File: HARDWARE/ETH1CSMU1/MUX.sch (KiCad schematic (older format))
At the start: 42 parts, among them J1401 Conn_01x03, K1401 MS05-1A87-75D, K1402 MS05-1A87-75D, K1403 MS05-1A87-75D, K1404 MS05-1A87-75D, K1405 MS05-1A87-75D, K1406 MS05-1A87-75D, K1407 MS05-1A87-75D, K1408 MS05-1A87-75D, K1409 MS05-1A87-75D, K1410 MS05-1A87-75D, K1411 MS05-1A87-75D, K1412 MS05-1A87-75D, K1413 MS05-1A87-75D, K1414 MS05-1A87-75D, K1415 MS05-1A87-75D, K1416 MS05-1A87-75D, K1417 MS05-1A87-75D, K1418 MS05-1A87-75D, K1419 G6KU-2F-Y, Q1401 BC847

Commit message: Schematic development
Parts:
- added C1301, C1302, C1303, C1304, C1305, C1306, C1307, C1308, C1309: 100n, symbol Device:C
- added R1301: R, symbol Device:R
- added U1301, U1302, U1303: TCA9534, symbol Interface_Expansion:TCA9534
- added U1304, U1305, U1306: ADG3308, symbol VoltageLevel_local:ADG3308
- added U1307: ULN2002, symbol Transistor_Array:ULN2002
- gave numbers to parts that had none: 2
- renumbered D1419 to D1301, D1401 to D1302, D1402 to D1303, D1403 to D1304, D1404 to D1305, D1405 to D1306, D1406 to D1307, D1407 to D1308, D1408 to D1309, D1409 to D1310, D1410 to D1311, D1411 to D1312, D1412 to D1313, D1413 to D1314, D1414 to D1315, D1415 to D1316, D1416 to D1317, D1417 to D1318, D1418 to D1319, J1401 to J1301, K1419 to K1301, K1401 to K1302, K1402 to K1303, K1403 to K1304, K1404 to K1305, K1405 to K1306, K1406 to K1307, K1407 to K1308, K1408 to K1309, K1409 to K1310, K1410 to K1311, K1411 to K1312, K1412 to K1313, K1413 to K1314, K1414 to K1315, K1415 to K1316, K1416 to K1317, K1417 to K1318, K1418 to K1319, Q1401 to Q1301
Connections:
- net +5V: now also C1301.1, C1302.1, C1303.1, U1304.20 (VCCY), U1305.20 (VCCY), U1306.20 (VCCY), U1307.9 (COM)
- net GND: now also C1301.2, C1302.2, C1303.2, C1304.2, C1305.2, C1306.2, C1307.2, C1308.2, C1309.2, U1301.2 (A1), U1301.3 (A2), U1301.8 (GND), U1302.1 (A0), U1302.3 (A2), U1302.8 (GND), U1303.3 (A2), U1303.8 (GND), U1304.11 (GND), U1305.11 (GND), U1306.11 (GND), U1307.8 (GND)
- net GUARD_A: now also U1308.16 (O1)
- net GUARD_B: now also U1308.15 (O2)
- net GUARD_C: now also U1308.14 (O3)
- net GUARD_D: now also U1308.13 (O4)
- net GUARD_E: now also U1308.12 (O5)
- net GUARD_F: now also U1308.11 (O6)
- net SEL_FRONT_REAR: now also R1301.2; no longer Q1301.1 (B)
- net STIM_A: now also U1307.16 (O1); no longer D1302.2 (A), K1302.3
- net STIM_B: now also U1307.15 (O2)
- net STIM_C: now also U1307.14 (O3)
- net STIM_D: now also U1307.13 (O4)
- net STIM_E: now also U1307.12 (O5)
- net STIM_F: now also U1307.11 (O6)
- net at U1308.1 (I1): now also U1305.19 (Y1)
- net at U1308.2 (I2): now also U1305.18 (Y2)
- net at U1308.3 (I3): now also U1305.17 (Y3)
- net at U1308.4 (I4): now also U1305.16 (Y4)
- net at U1308.5 (I5): now also U1305.15 (Y5)
- net at U1308.6 (I6): now also U1305.14 (Y6)
- net at U1309.1 (I1): now also U1306.19 (Y1)
- net GND_F: now reaches U1309.11 (O6)
- net GND_E: now reaches U1309.12 (O5)
- net GND_D: now reaches U1309.13 (O4)
- net GND_C: now reaches U1309.14 (O3)
- net GND_B: now reaches U1309.15 (O2)
- net GND_A: now reaches U1309.16 (O1)
- net GND_A: now also D1302.2 (A), K1302.3
- net at U1309.2 (I2): now also U1306.18 (Y2)
- net at U1309.3 (I3): now also U1306.17 (Y3)
- net at U1309.4 (I4): now also U1306.16 (Y4)
- net at U1309.5 (I5): now also U1306.15 (Y5)
- net at U1309.6 (I6): now also U1306.14 (Y6)
- new net: U1301.10 (P5), U1304.7 (A6)
- new net: U1301.4 (P0), U1304.2 (A1)
- new net: U1301.5 (P1), U1304.3 (A2)
- new net: U1301.6 (P2), U1304.4 (A3)
- new net: U1301.7 (P3), U1304.5 (A4)
- new net: U1301.9 (P4), U1304.6 (A5)
- new net: U1304.19 (Y1), U1307.1 (I1)
- new net: U1304.18 (Y2), U1307.2 (I2)
- new net: U1304.17 (Y3), U1307.3 (I3)
- new net: U1304.16 (Y4), U1307.4 (I4)
- new net: U1304.15 (Y5), U1307.5 (I5)
- new net: U1304.14 (Y6), U1307.6 (I6)
- new net: U1302.10 (P5), U1305.7 (A6)
- new net: U1302.4 (P0), U1305.2 (A1)
- new net: U1302.5 (P1), U1305.3 (A2)
- new net: U1302.6 (P2), U1305.4 (A3)
- new net: U1302.7 (P3), U1305.5 (A4)
- new net: U1302.9 (P4), U1305.6 (A5)
- new net: U1303.4 (P0), U1306.2 (A1)
- new net: U1303.5 (P1), U1306.3 (A2)
- new net: U1303.6 (P2), U1306.4 (A3)
- new net: U1303.7 (P3), U1306.5 (A4)
- new net: U1303.9 (P4), U1306.6 (A5)
- new net: U1303.10 (P5), U1306.7 (A6)
- new net: Q1301.1 (B), R1301.1
- new net +3V3: C1304.1, C1305.1, C1306.1, C1307.1, C1308.1, C1309.1, U1301.1 (A0), U1301.16 (VDD), U1302.16 (VDD), U1302.2 (A1), U1303.1 (A0), U1303.16 (VDD), U1303.2 (A1), U1304.1 (VCCA), U1304.10 (EN), U1305.1 (VCCA), U1305.10 (EN), U1306.1 (VCCA), U1306.10 (EN)
- new net SECOND-I2C1_SCL: U1301.14 (SCL), U1302.14 (SCL), U1303.14 (SCL)
- new net SECOND-I2C1_SDA: U1301.15 (SDA), U1302.15 (SDA), U1303.15 (SDA)
- no-connect marks 0 -> 24
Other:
- moved on the sheet: D1301, D1302, D1303, D1304, D1305, D1306, D1307, D1308, D1309, D1310, D1311, D1312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

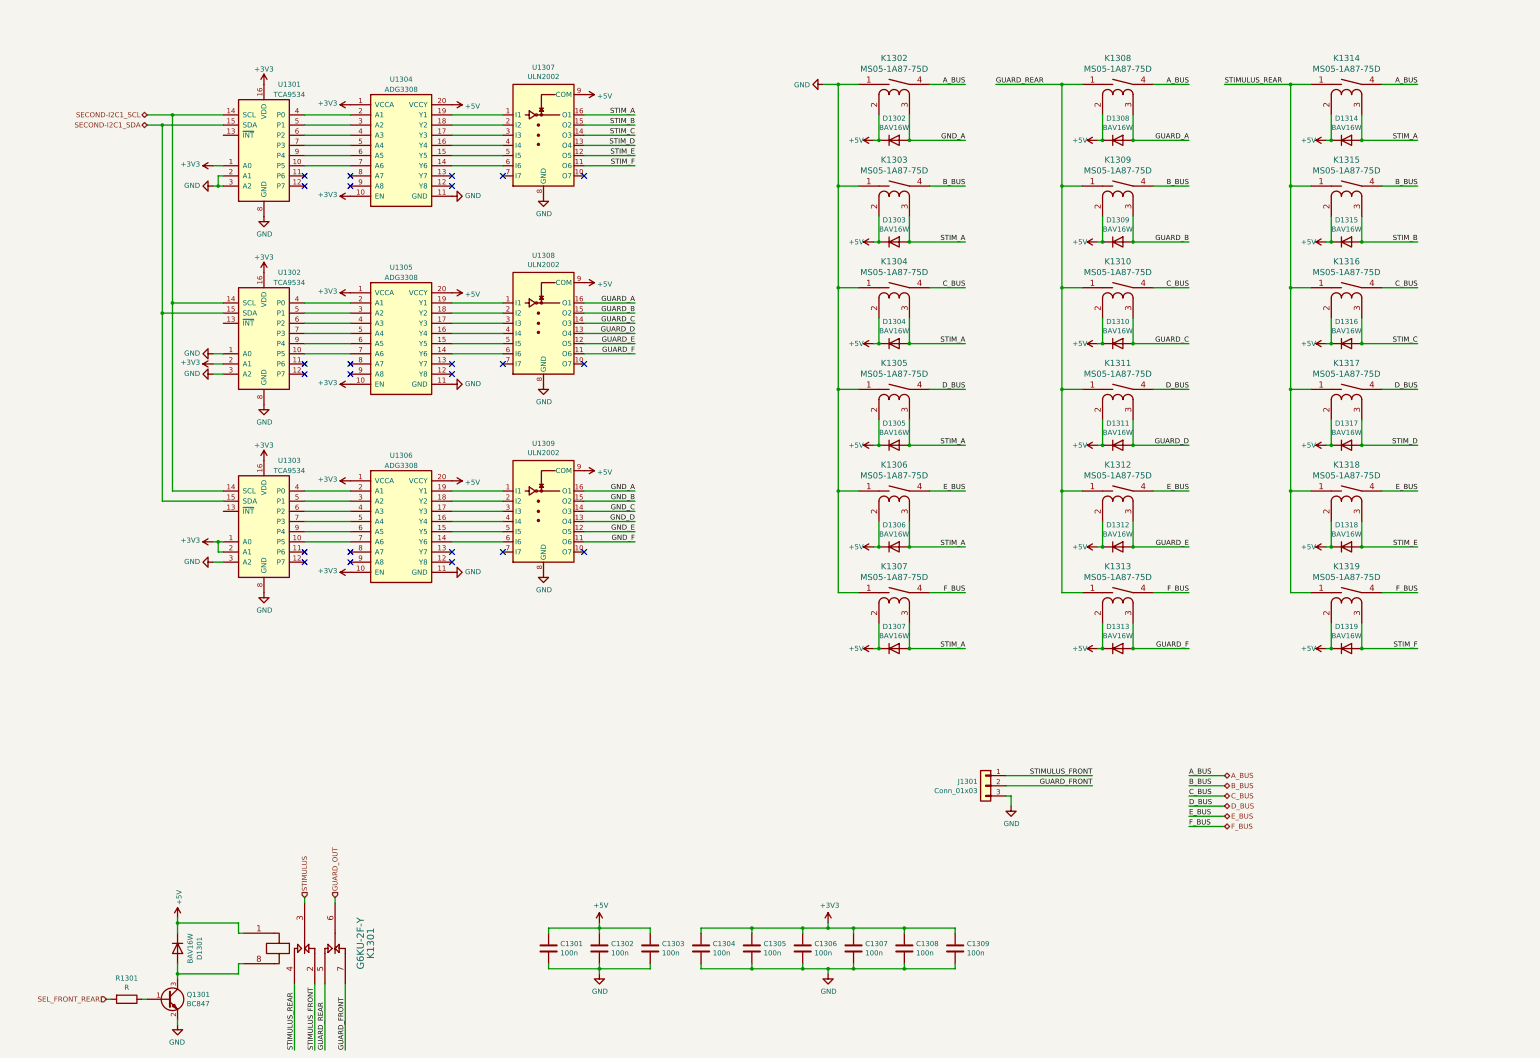
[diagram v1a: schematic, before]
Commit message: Changed BUS mux schematic
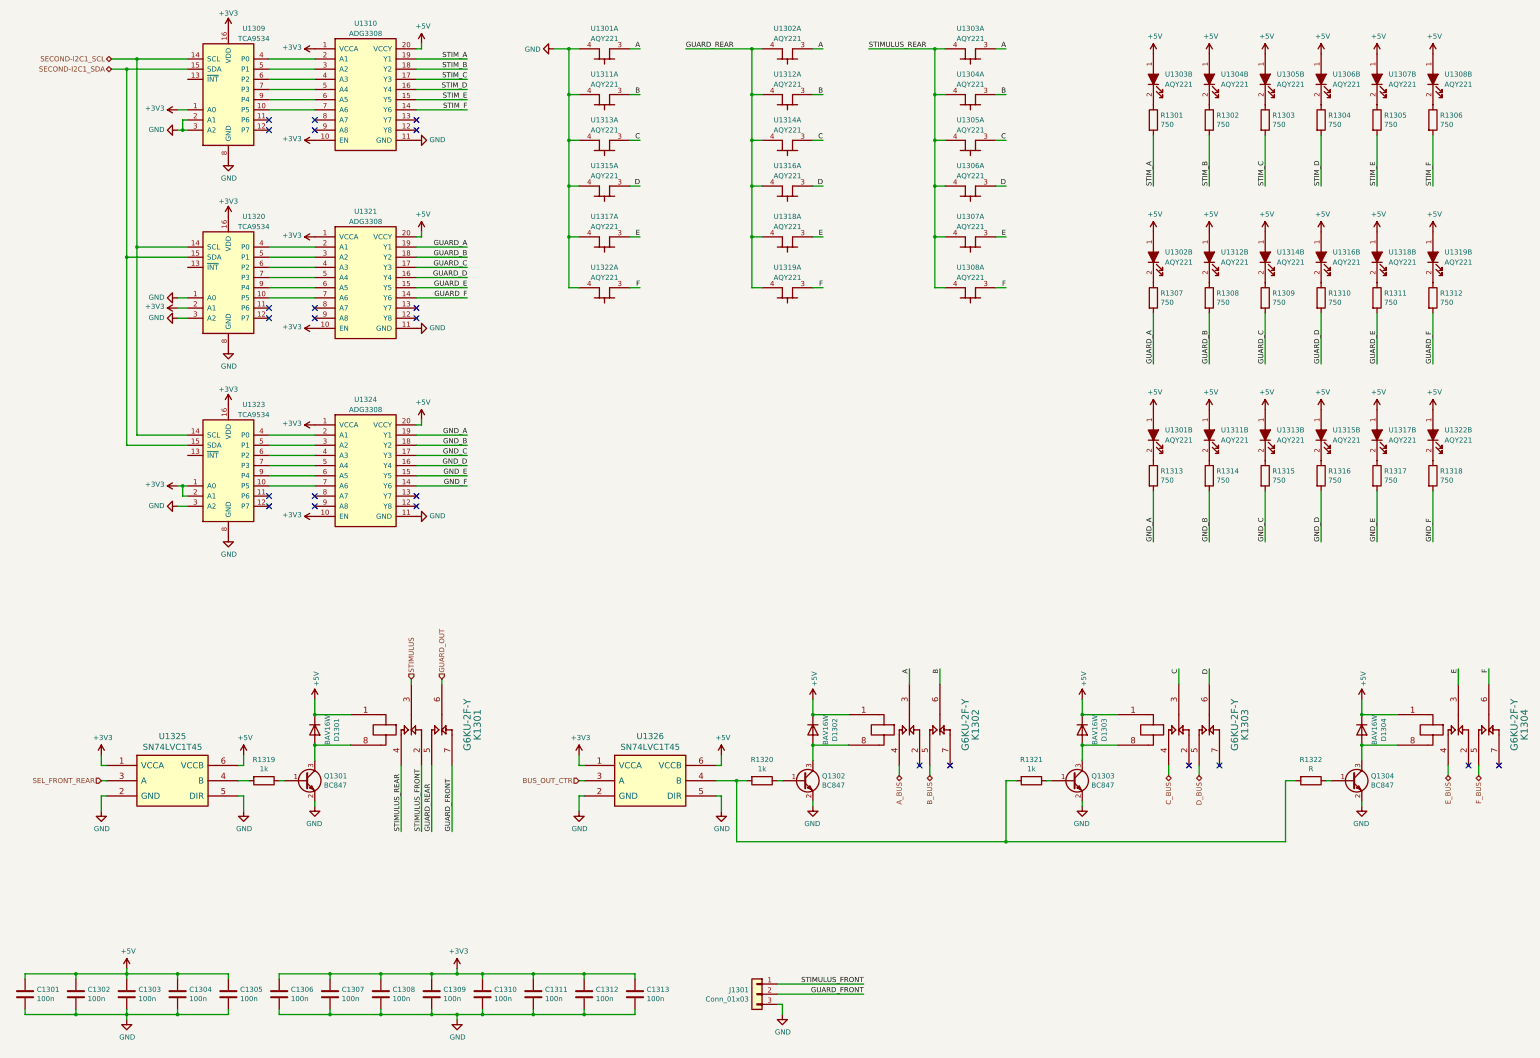
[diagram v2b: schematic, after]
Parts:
- removed D1305, D1306, D1307, D1308, D1309, D1310, D1311, D1312, D1313, D1314, D1315, D1316, D1317, D1318, D1319: BAV16W, Diodes_SMD:D_SOD-323_HandSoldering, symbol Device:D
- removed K1302, K1303, K1304, K1305, K1306, K1307, K1308, K1309, K1310, K1311, K1312, K1313, K1314, K1315, K1316, K1317, K1318, K1319: MS05-1A87-75D, THT:MS05-1A87-75D_Socket, symbol relay_local:MS05-1A87-75D
- removed U1307, U1308, U1309: ULN2002, symbol Transistor_Array:ULN2002
- added C1304, C1305, C1312, C1313: 100n, symbol Device:C
- added K1302, K1303, K1304: G6KU-2F-Y, symbol relay_local:G6KU-2F-Y
- added Q1302, Q1303, Q1304: BC847, Package_TO_SOT_SMD:SOT-23, symbol Transistor_BJT:BC847
- added R1301, R1302, R1303, R1304, R1305, R1306, R1307, R1308, R1309, R1310, R1311, R1312, R1313, R1314, R1315, R1316, R1317, R1318: 750, symbol Device:R
- added R1320, R1321: 1k, symbol Device:R
- added R1322: R, symbol Device:R
- added U1301, U1302, U1303, U1304, U1305, U1306, U1307, U1308, U1311, U1312, U1313, U1314, U1315, U1316, U1317, U1318, U1319, U1322: AQY221, SMD:AQY2, symbol relay_local:AQY221
- added U1325, U1326: SN74LVC1T45, SMD:SC70-6, symbol logic_local:SN74LVC1T45
- R1319: renamed from R1301; value R -> 1k
- renumbered C1304 to C1306, C1305 to C1307, C1306 to C1308, C1307 to C1309, C1308 to C1310, C1309 to C1311, U1301 to U1309, U1304 to U1310, U1302 to U1320, U1305 to U1321, U1303 to U1323, U1306 to U1324
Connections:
- net +3V3: now also C1312.1, C1313.1, U1325.1 (VCCA), U1326.1 (VCCA)
- net +5V: now also C1304.1, C1305.1, K1302.1, K1303.1, K1304.1, U1301.1, U1302.1, U1303.1, U1304.1, U1305.1, U1306.1, U1307.1, U1308.1, U1311.1, U1312.1, U1313.1, U1314.1, U1315.1, U1316.1, U1317.1, U1318.1, U1319.1, U1322.1, U1325.6 (VCCB), U1326.6 (VCCB)
- net A_BUS: now also K1302.4
- net B_BUS: now also K1302.5
- net C_BUS: now also K1303.4
- net D_BUS: now also K1303.5
- net E_BUS: now also K1304.4
- net F_BUS: now also K1304.5
- net GND: now also C1304.2, C1305.2, C1312.2, C1313.2, Q1302.2 (E), Q1303.2 (E), Q1304.2 (E), U1301.4, U1311.4, U1313.4, U1315.4, U1317.4, U1322.4, U1325.2 (GND), U1325.5 (DIR), U1326.2 (GND), U1326.5 (DIR)
- net GND_A: now also U1324.19 (Y1), R1313.2; no longer D1302.2 (A)
- net GND_B: now also U1324.18 (Y2), R1314.2
- net GND_C: now also U1324.17 (Y3), R1315.2
- net GND_D: now also U1324.16 (Y4), R1316.2
- net GND_E: now also U1324.15 (Y5), R1317.2
- net GND_F: now also U1324.14 (Y6), R1318.2
- net GUARD_A: now also U1321.19 (Y1), R1307.2
- net GUARD_B: now also U1321.18 (Y2), R1308.2
- net GUARD_C: now also U1321.17 (Y3), R1309.2
- net GUARD_D: now also U1321.16 (Y4), R1310.2
- net GUARD_E: now also U1321.15 (Y5), R1311.2
- net GUARD_F: now also U1321.14 (Y6), R1312.2
- net GUARD_REAR: now also U1302.4, U1312.4, U1314.4, U1316.4, U1318.4, U1319.4
- net SEL_FRONT_REAR: now also U1325.3 (A); no longer R1319.2
- net STIMULUS_REAR: now also U1303.4, U1304.4, U1305.4, U1306.4, U1307.4, U1308.4
- net STIM_A: now also U1310.19 (Y1), R1301.2; no longer D1303.2 (A), D1304.2 (A)
- net STIM_B: now also U1310.18 (Y2), R1302.2
- net STIM_C: now also U1310.17 (Y3), R1303.2
- net STIM_D: now also U1310.16 (Y4), R1304.2
- net STIM_E: now also U1310.15 (Y5), R1305.2
- net STIM_F: now also U1310.14 (Y6), R1306.2
- new net: R1318.1, U1322.2
- new net: R1317.1, U1317.2
- new net: R1316.1, U1315.2
- new net: R1315.1, U1313.2
- new net: R1314.1, U1311.2
- new net: R1313.1, U1301.2
- new net: R1319.2, U1325.4 (B)
- new net: R1309.1, U1314.2
- new net: R1308.1, U1312.2
- new net: R1307.1, U1302.2
- new net: R1312.1, U1319.2
- new net: R1311.1, U1318.2
- new net: R1310.1, U1316.2
- new net: R1301.1, U1303.2
- new net: R1303.1, U1305.2
- new net: R1302.1, U1304.2
- new net: R1304.1, U1306.2
- new net: R1306.1, U1308.2
- new net: R1305.1, U1307.2
- new net: D1302.2 (A), K1302.8, Q1302.3 (C)
- new net: Q1302.1 (B), R1320.1
- new net: R1320.2, R1321.2, R1322.2, U1326.4 (B)
- new net: D1303.2 (A), K1303.8, Q1303.3 (C)
- new net: Q1303.1 (B), R1321.1
- new net: D1304.2 (A), K1304.8, Q1304.3 (C)
- new net: Q1304.1 (B), R1322.1
- new net A: K1302.3 (C1), U1301.3, U1302.3, U1303.3
- new net B: K1302.6, U1304.3, U1311.3, U1312.3
- new net BUS_OUT_CTR: U1326.3 (A)
- new net C: K1303.3 (C1), U1305.3, U1313.3, U1314.3
- new net D: K1303.6, U1306.3, U1315.3, U1316.3
- new net E: K1304.3 (C1), U1307.3, U1317.3, U1318.3
- new net F: K1304.6, U1308.3, U1319.3, U1322.3
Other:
- moved on the sheet: C1301, C1302, C1303, C1306, C1307, C1308, C1309, C1310, C1311, D1301, J1301, K1301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

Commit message: check in
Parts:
- C1301, C1302, C1303, C1304, C1305, C1306, C1307, C1308, C1309, C1310, C1311, C1312, C1313: footprint (none) -> SMD:C_0603_Symbol1
- J1301: footprint (none) -> THT:GMSTB_2.5 3-GF-7.62
- K1301, K1302, K1303, K1304: footprint (none) -> SMD:G6K-2F
- R1301, R1302, R1303, R1304, R1305, R1306, R1307, R1308, R1309, R1310, R1311, R1312, R1313, R1314, R1315, R1316, R1317, R1318: footprint (none) -> SMD:R_0603_Symbol8
- R1319, R1320, R1321: footprint (none) -> SMD:R_0603_Symbol9
- R1322: value R -> 1k; footprint (none) -> SMD:R_0603_Symbol9
- U1309, U1320, U1323: footprint (none) -> Housings_SSOP:TSSOP-16_4.4x5mm_Pitch0.65mm
- U1310, U1321, U1324: footprint (none) -> Housings_SSOP:SSOP-20_4.4x6.5mm_Pitch0.65mm
